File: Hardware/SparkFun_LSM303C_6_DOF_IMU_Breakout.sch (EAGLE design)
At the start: 26 parts, among them Q1 2.5A/30V, U1 LSM303C, U2 LM3880

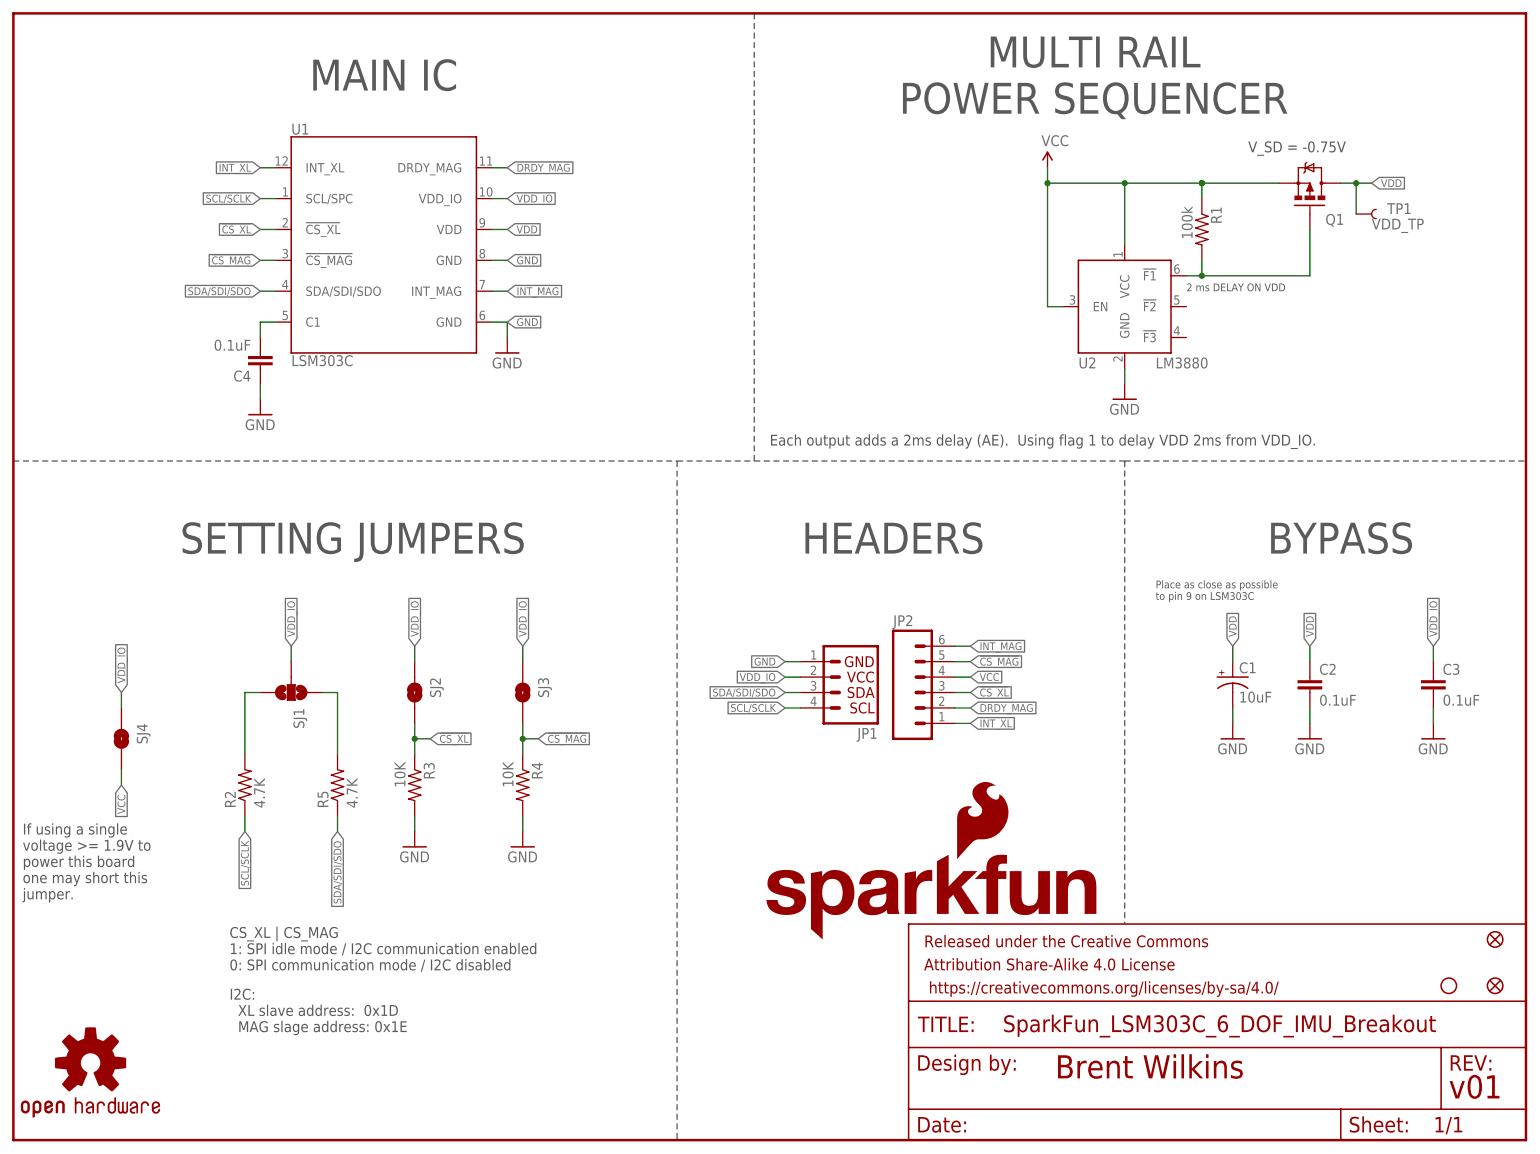
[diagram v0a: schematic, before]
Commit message: Addded another mounting hole, removed documentation, & made I2C by default
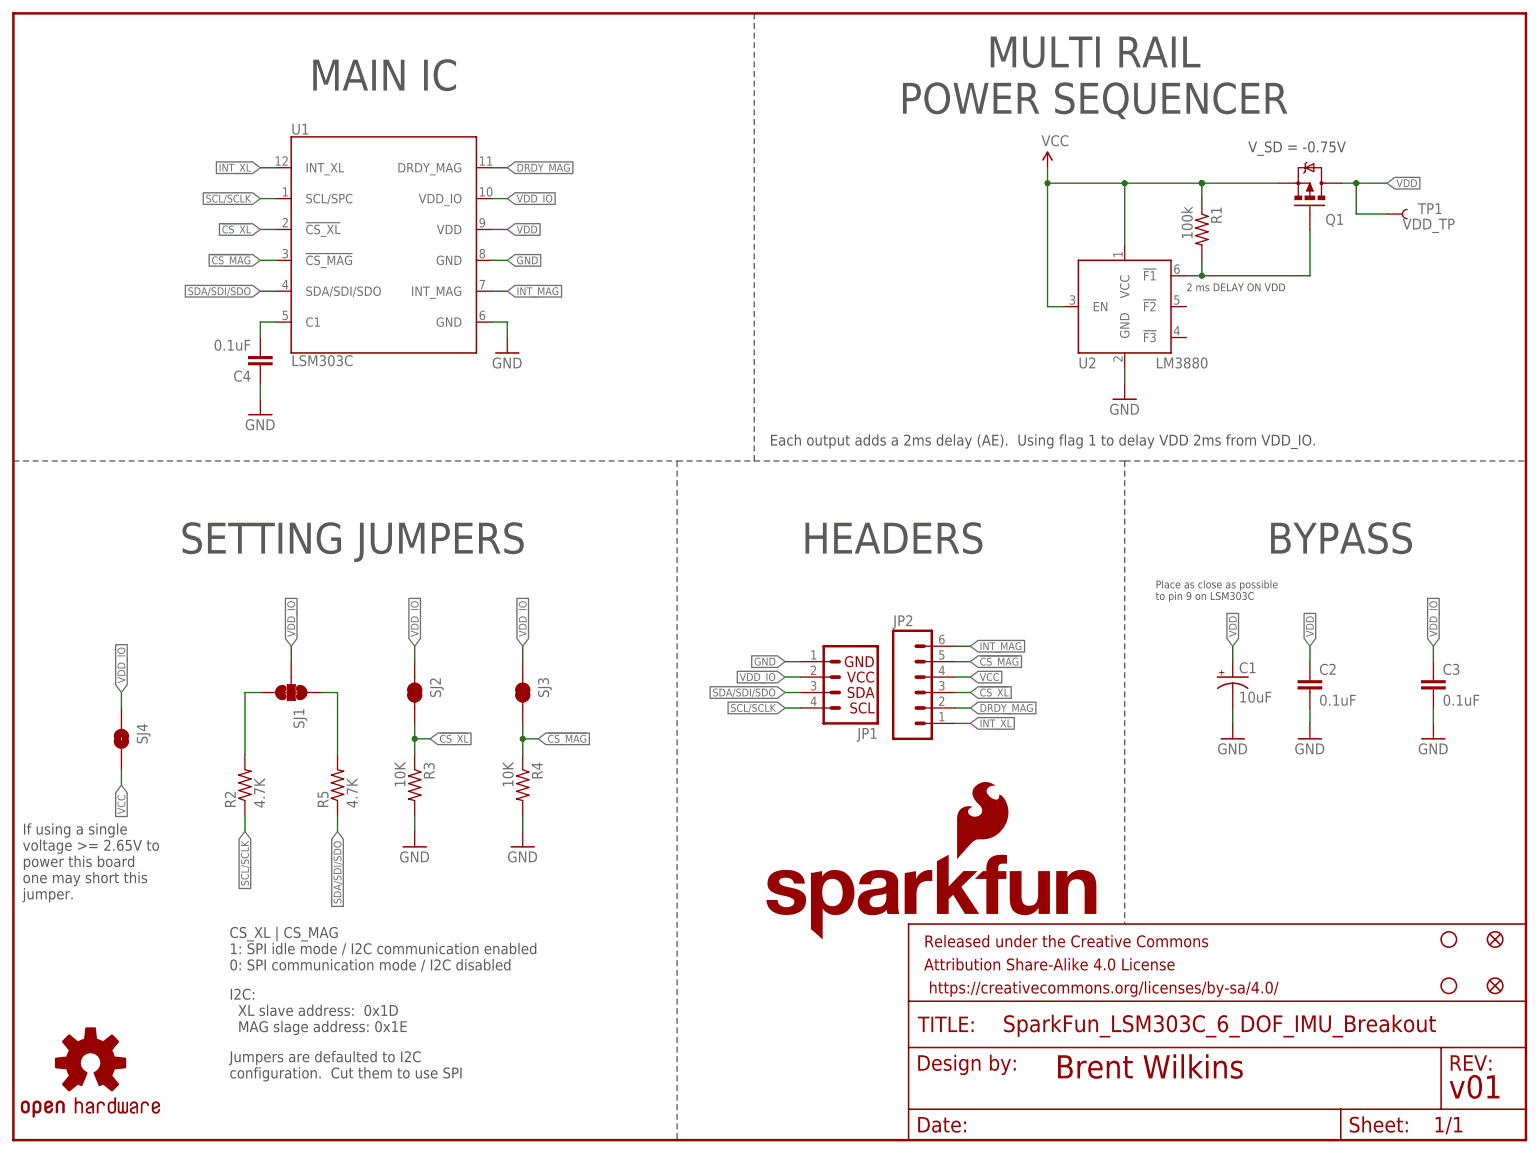
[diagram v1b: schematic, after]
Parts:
- added STANDOFF2: STAND-OFF, SparkFun-Electromechanical:STAND-OFF
- SJ1: value JUMPER-PAD-3-NOYES_SILK -> (none); device SparkFun-Passives:JUMPER-PAD-3-NOYES_SILK -> SparkFun-Passives:JUMPER-PAD-3-NC_BY_TRACE
- SJ2, SJ3: value JUMPER-PAD-2-NO -> JUMPER-PAD-2-NC_BY_TRACE; device SparkFun-Passives:JUMPER-PAD-2-NO -> SparkFun-Passives:JUMPER-PAD-2-NC_BY_TRACE
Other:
- note added: "If using a single voltage >= 2.65V to power this board one may short this jumper."
- note added: "Jumpers are defaulted to I2C configuration. Cut them to use SPI"
- note removed: "If using a single voltage >= 1.9V to power this board one may short this jumper."
- moved on the sheet: TP1
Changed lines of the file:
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@@
 <part name="R3" library="SparkFun-Resistors" deviceset="10KOHM-1/10W-1%(0603)" device="0603" value="10K"/>
 <part name="R4" library="SparkFun-Resistors" deviceset="10KOHM-1/10W-1%(0603)" device="0603" value="10K"/>
-<part name="SJ2" library="SparkFun-Passives" deviceset="JUMPER-PAD-2-NO" device=""/>
-<part name="SJ3" library="SparkFun-Passives" deviceset="JUMPER-PAD-2-NO" device=""/>
+<part name="SJ2" library="SparkFun-Passives" deviceset="JUMPER-PAD-2-NC_BY_TRACE" device=""/>
+<part name="SJ3" library="SparkFun-Passives" deviceset="JUMPER-PAD-2-NC_BY_TRACE" device=""/>
 <part name="JP2" library="SparkFun-Connectors" deviceset="M06" device="SILK_FEMALE_PTH"/>
 <part name="LOGO1" library="SparkFun-Aesthetics" deviceset="SFE_LOGO_NAME" device=".1_INCH" value="SFE_LOGO_NAME.1_INCH"/>
@@
 <part name="JP1" library="SparkFun-Connectors" deviceset="I2C_STANDARD" device=""/>
 <part name="SUPPLY2" library="SparkFun-Aesthetics" deviceset="VCC" device=""/>
-<part name="SJ1" library="SparkFun-Passives" deviceset="JUMPER-PAD-3-NO" device="YES_SILK"/>
+<part name="SJ1" library="SparkFun-Passives" deviceset="JUMPER-PAD-3-NC_BY_TRACE" device=""/>
 <part name="SJ4" library="SparkFun-Passives" deviceset="JUMPER-PAD-2-NO" device=""/>
 <part name="TP1" library="SparkFun-Passives" deviceset="TEST-POINT" device="TP_15TH_THRU" value="VDD_TP"/>
 <part name="STANDOFF1" library="SparkFun-Electromechanical" deviceset="STAND-OFF" device=""/>
+<part name="STANDOFF2" library="SparkFun-Electromechanical" deviceset="STAND-OFF" device=""/>
 </parts>
 <sheets>
@@
 <text x="203.2" y="162.56" size="1.778" layer="97">V_SD = -0.75V</text>
 <text x="1.524" y="52.07" size="1.778" layer="97" font="vector" align="top-left">If using a single
-voltage &gt;= 1.9V to
+voltage &gt;= 2.65V to
 power this board
 one may short this
 jumper.
 </text>
+<text x="35.56" y="10.16" size="1.778" layer="97" font="vector">Jumpers are defaulted to I2C
+configuration.  Cut them to use SPI</text>
 </plain>
 <instances>
@@
 <attribute name="NAME" x="20.32" y="68.58" size="1.778" layer="95" rot="R270"/>
 </instance>
-<instance part="TP1" gate="G$1" x="220.98" y="152.4" smashed="yes">
-<attribute name="NAME" x="226.06" y="152.4" size="1.778" layer="95"/>
-<attribute name="VALUE" x="223.52" y="149.86" size="1.778" layer="96"/>
+<instance part="TP1" gate="G$1" x="226.06" y="152.4" smashed="yes">
+<attribute name="NAME" x="231.14" y="152.4" size="1.778" layer="95"/>
+<attribute name="VALUE" x="228.6" y="149.86" size="1.778" layer="96"/>
 </instance>
 <instance part="STANDOFF1" gate="G$1" x="236.22" y="25.4"/>
+<instance part="STANDOFF2" gate="G$1" x="236.22" y="33.02"/>
 </instances>
 <busses>
@@
 <wire x1="78.74" y1="134.62" x2="81.28" y2="134.62" width="0.1524" layer="91"/>
 <wire x1="81.28" y1="134.62" x2="81.28" y2="132.08" width="0.1524" layer="91"/>
-<label x="81.28" y="134.62" size="1.27" layer="95" xref="yes"/>
 </segment>
 <segment>
@@
 <pinref part="Q1" gate="G$1" pin="D"/>
 <wire x1="218.44" y1="157.48" x2="220.98" y2="157.48" width="0.1524" layer="91"/>
-<label x="223.52" y="157.48" size="1.27" layer="95" xref="yes"/>
+<label x="226.06" y="157.48" size="1.27" layer="95" xref="yes"/>
 <pinref part="TP1" gate="G$1" pin="1"/>
-<wire x1="220.98" y1="157.48" x2="223.52" y2="157.48" width="0.1524" layer="91"/>
+<wire x1="220.98" y1="157.48" x2="226.06" y2="157.48" width="0.1524" layer="91"/>
+<wire x1="226.06" y1="152.4" x2="220.98" y2="152.4" width="0.1524" layer="91"/>
 <wire x1="220.98" y1="152.4" x2="220.98" y2="157.48" width="0.1524" layer="91"/>
 <junction x="220.98" y="157.48"/>

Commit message: Added PROD-IDs to all placed parts
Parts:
- R1: PROD_ID (none) -> RES-07828
- U1: PROD_ID (none) -> IC-12557
- U2: PROD_ID (none) -> IC-12558
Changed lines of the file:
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@@
 <attribute name="DESIGNER" value="Brent Wilkins"/>
 </part>
-<part name="U1" library="SparkFun-DigitalIC" deviceset="LSM303C" device=""/>
+<part name="U1" library="SparkFun-DigitalIC" deviceset="LSM303C" device="">
+<attribute name="PROD_ID" value="IC-12557"/>
+</part>
 <part name="C4" library="SparkFun-Capacitors" deviceset="0.1UF-25V(+80/-20%)(0603)" device="" value="0.1uF"/>
 <part name="GND15" library="SparkFun-Aesthetics" deviceset="GND" device=""/>
 <part name="GND13" library="SparkFun-Aesthetics" deviceset="GND" device=""/>
 <part name="Q1" library="SparkFun-DiscreteSemi" deviceset="MOSFET-PCHANNEL" device="DMG2307L" value="2.5A/30V"/>
-<part name="R1" library="SparkFun-Passives" deviceset="RESISTOR" device="0603-RES" value="100k"/>
-<part name="U2" library="SparkFun-DigitalIC" deviceset="LM3880/-QI" device="" value="LM3880"/>
+<part name="R1" library="SparkFun-Passives" deviceset="RESISTOR" device="0603-RES" value="100k">
+<attribute name="PROD_ID" value="RES-07828"/>
+</part>
+<part name="U2" library="SparkFun-DigitalIC" deviceset="LM3880/-QI" device="" value="LM3880">
+<attribute name="PROD_ID" value="IC-12558"/>
+</part>
 <part name="GND14" library="SparkFun-Aesthetics" deviceset="GND" device=""/>
 <part name="C3" library="SparkFun-Capacitors" deviceset="0.1UF-25V(+80/-20%)(0603)" device="" value="0.1uF"/>
@@
 <instance part="FRAME1" gate="G$1" x="0" y="0"/>
 <instance part="FRAME1" gate="V" x="147.32" y="0"/>
-<instance part="U1" gate="G$1" x="60.96" y="147.32"/>
+<instance part="U1" gate="G$1" x="60.96" y="147.32">
+<attribute name="PROD_ID" x="60.96" y="147.32" size="1.778" layer="96" display="off"/>
+</instance>
 <instance part="C4" gate="G$1" x="40.64" y="129.54" rot="R180"/>
 <instance part="GND15" gate="1" x="40.64" y="119.38"/>
@@
 <attribute name="NAME" x="215.9" y="152.4" size="1.778" layer="95" rot="MR180"/>
 </instance>
-<instance part="R1" gate="G$1" x="195.58" y="149.86" rot="R270"/>
+<instance part="R1" gate="G$1" x="195.58" y="149.86" rot="R270">
+<attribute name="PROD_ID" x="195.58" y="149.86" size="1.778" layer="96" rot="R270" display="off"/>
+</instance>
 <instance part="U2" gate="G$1" x="182.88" y="137.16" smashed="yes">
 <attribute name="NAME" x="175.26" y="127" size="1.778" layer="95"/>

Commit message: Silk work
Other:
- note added: "VCC = 2.65V to 4.3V"
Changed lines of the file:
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@@
 <text x="35.56" y="10.16" size="1.778" layer="97" font="vector">Jumpers are defaulted to I2C
 configuration.  Cut them to use SPI</text>
+<text x="134.62" y="157.48" size="1.9304" layer="97">VCC = 2.65V to 4.3V</text>
 </plain>
 <instances>

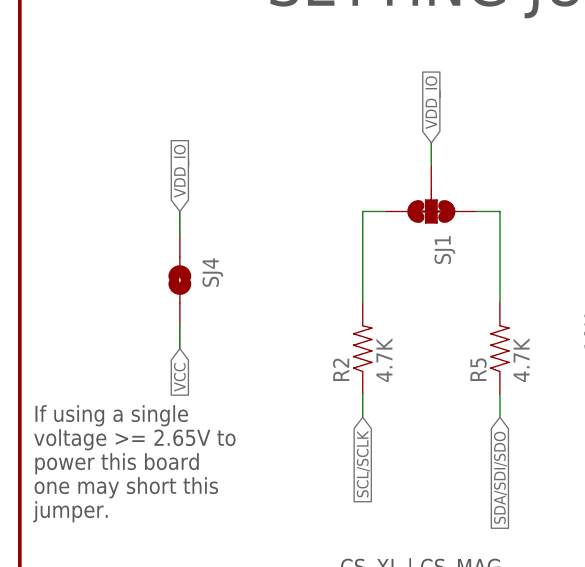
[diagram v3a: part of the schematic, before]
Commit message: Closed VDD-VDD_IO jumper making the PCBA single input volatage (3.3V) by default
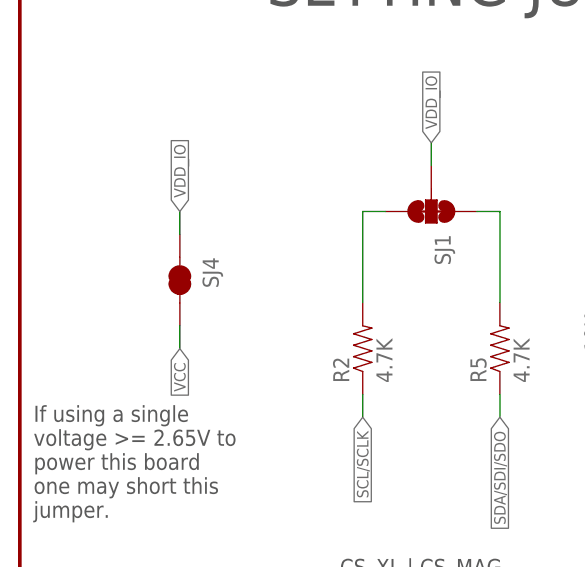
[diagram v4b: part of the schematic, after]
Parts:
- SJ4: value JUMPER-PAD-2-NO -> JUMPER-PAD-2-NC_BY_TRACE; device SparkFun-Passives:JUMPER-PAD-2-NO -> SparkFun-Passives:JUMPER-PAD-2-NC_BY_TRACE
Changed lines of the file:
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@@
 <part name="SUPPLY2" library="SparkFun-Aesthetics" deviceset="VCC" device=""/>
 <part name="SJ1" library="SparkFun-Passives" deviceset="JUMPER-PAD-3-NC_BY_TRACE" device=""/>
-<part name="SJ4" library="SparkFun-Passives" deviceset="JUMPER-PAD-2-NO" device=""/>
+<part name="SJ4" library="SparkFun-Passives" deviceset="JUMPER-PAD-2-NC_BY_TRACE" device=""/>
 <part name="TP1" library="SparkFun-Passives" deviceset="TEST-POINT" device="TP_15TH_THRU" value="VDD_TP"/>
 <part name="STANDOFF1" library="SparkFun-Electromechanical" deviceset="STAND-OFF" device=""/>
